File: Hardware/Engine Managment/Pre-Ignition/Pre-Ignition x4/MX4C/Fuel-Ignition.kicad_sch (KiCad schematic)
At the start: 45 parts, among them Q1 IRFR024, Q2 IRFR024, Q3 IRFR024, Q4 IRFR024, U2 TC4424, U3 TC4424

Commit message: Upload correct initial upload files
Initial upload files were accidently taken from an alpha folder. 5v pins on main connector had no voltage. To fix the issue on any manufactured boards remove C8 and C9. Then short the pins of the removed capacitors.
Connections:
- net IGN-V: no longer names the net of C10.1, C11.1, JP3.2 (C), U2.6 (V+), U3.6 (V+)
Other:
- moved on the sheet: C10, C11, IGN1, IGN2, IGN3, IGN4, JP3, R22, R23, R24, R25, R28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

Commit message: Structure Update
MX2 - RevB Upload
MX4B-2 - KiCad Version update (no changes)
MX4C - Organized Schematic, Minor layout change
Engine Simulator 8 Channel - Organized Schematic (no changes)
PMAP-M - Map Sensor Breakout for MX4C
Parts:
- renumbered C11 to C10, C10 to C9, D9 to D10, D10 to D11, D11 to D12, D12 to D13, D13 to D14, D6 to D7, D7 to D8, D8 to D9, JP3 to JP6, R7 to R3, R8 to R4, R9 to R5, R10 to R6
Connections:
- net IGN-PWR: now reaches C10.1, C9.1, JP6.2 (C), U2.6 (V+), U3.6 (V+)
- net VDD renamed +5V
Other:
- moved on the sheet: C10, C9, D10, D11, D12, D13, D14, D7, D8, D9, IGN1, IGN2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

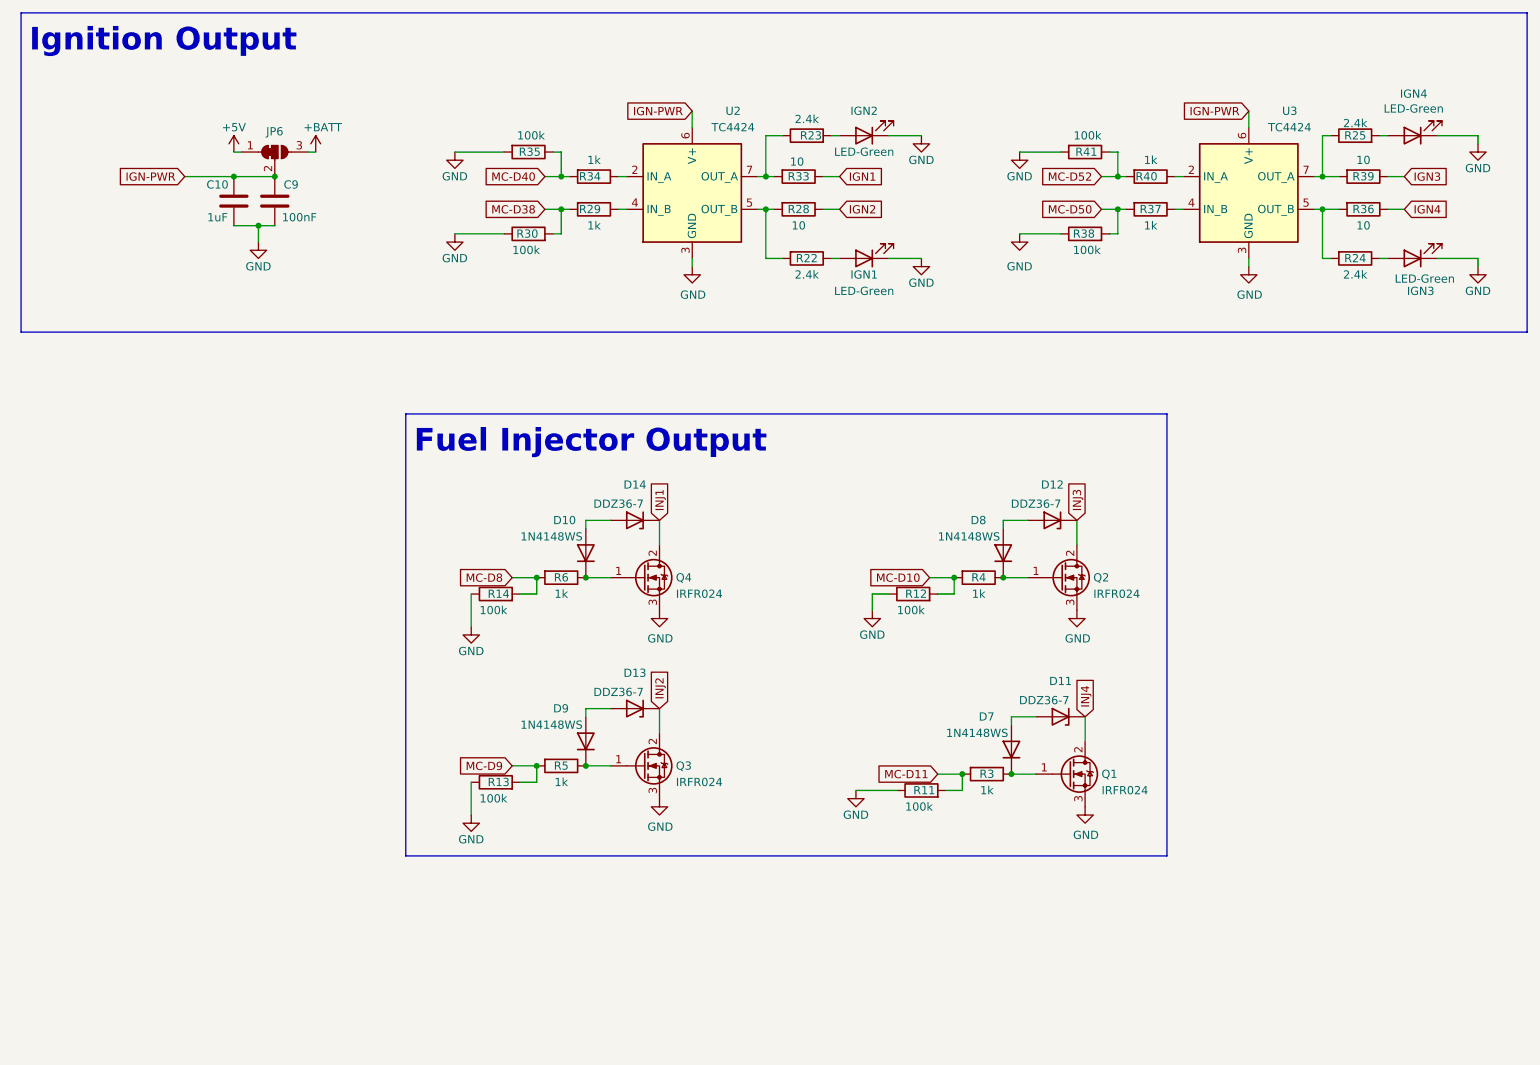
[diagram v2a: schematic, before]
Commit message: minor update
Copper Pour and clearances updated.
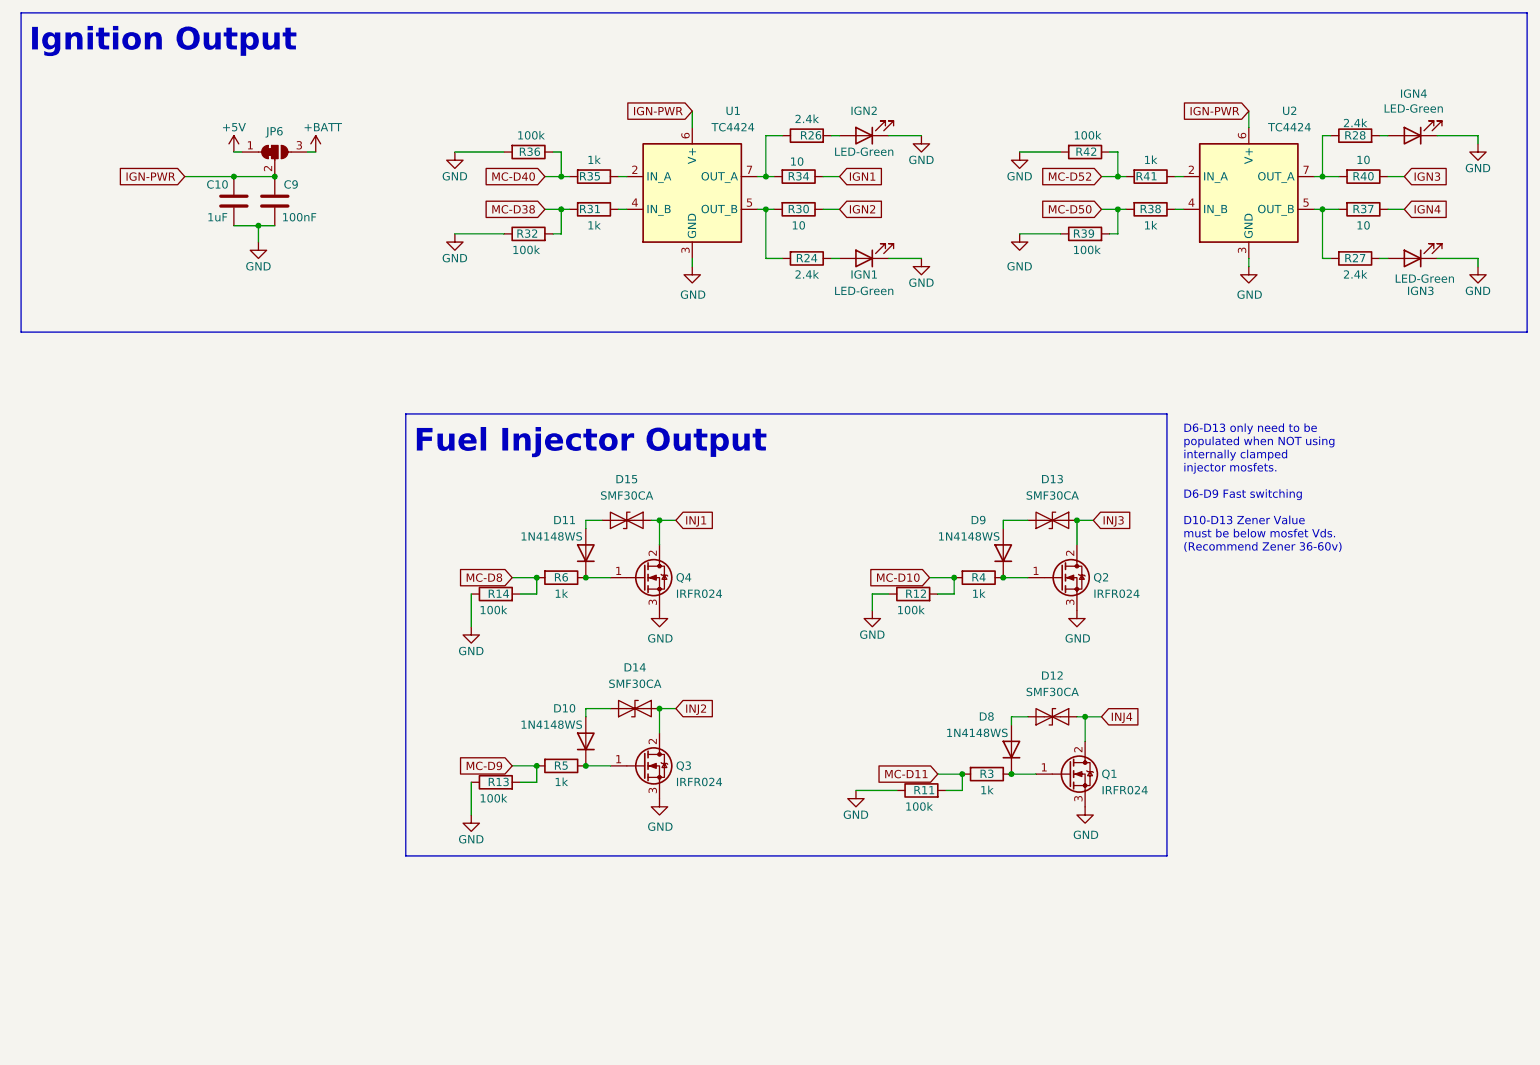
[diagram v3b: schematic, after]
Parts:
- removed D11, D12, D13, D14: DDZ36-7, Diode_SMD:D_SOD-123, symbol Diode:BZX84Cxx
- added D12, D13, D14, D15: SMF30CA, Diode_SMD:D_SOD-123F, symbol Detonation:SMAJ30CA
- renumbered D9 to D10, D10 to D11, D7 to D8, D8 to D9, R22 to R24, R23 to R26, R24 to R27, R25 to R28, R28 to R30, R29 to R31, R30 to R32, R33 to R34, R34 to R35, R35 to R36, R36 to R37, R37 to R38, R38 to R39, R39 to R40, R40 to R41, R41 to R42, U2 to U1, U3 to U2
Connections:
- net INJ1: now also D15.1 (A1)
- net INJ2: now also D14.1 (A1)
- net INJ3: now also D13.1 (A1)
- net INJ4: now also D12.1 (A1)
- net at D11.2 (A): now also D15.2 (A2)
- net at D9.2 (A): now also D13.2 (A2)
- net at D8.2 (A): now also D12.2 (A2)
- net at D10.2 (A): now also D14.2 (A2)
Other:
- note added: "D6-D13 only need to be populated when NOT using internally clamped injector mosfets. D6-D9 Fast switching D10-D13 Zener Value must be below mosfet Vds. (Recommend Zener 36-60v)"
